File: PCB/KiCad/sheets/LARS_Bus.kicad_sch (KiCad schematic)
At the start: 24 parts, among them J27 USB1, J28 USB2, U11 USBLC6-2SC6, U12 TCAN1057AVDRQ1, U13 USBLC6-2SC6

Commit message: reannotate schematic
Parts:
- renumbered C63 to C65, C64 to C66, C65 to C67, J27 to J28, J28 to J29, U11 to U10, U12 to U11, U13 to U12
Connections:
- net CAN1_HIGH renamed CAN1_P
- net CAN1_LOW renamed CAN1_N

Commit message: finish PCB routing
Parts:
- C67: value 1u -> 2u2
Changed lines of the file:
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@@
 			)
 		)
-		(property "Value" "1u"
+		(property "Value" "2u2"
 			(at 98.298 148.082 0)
 			(effects

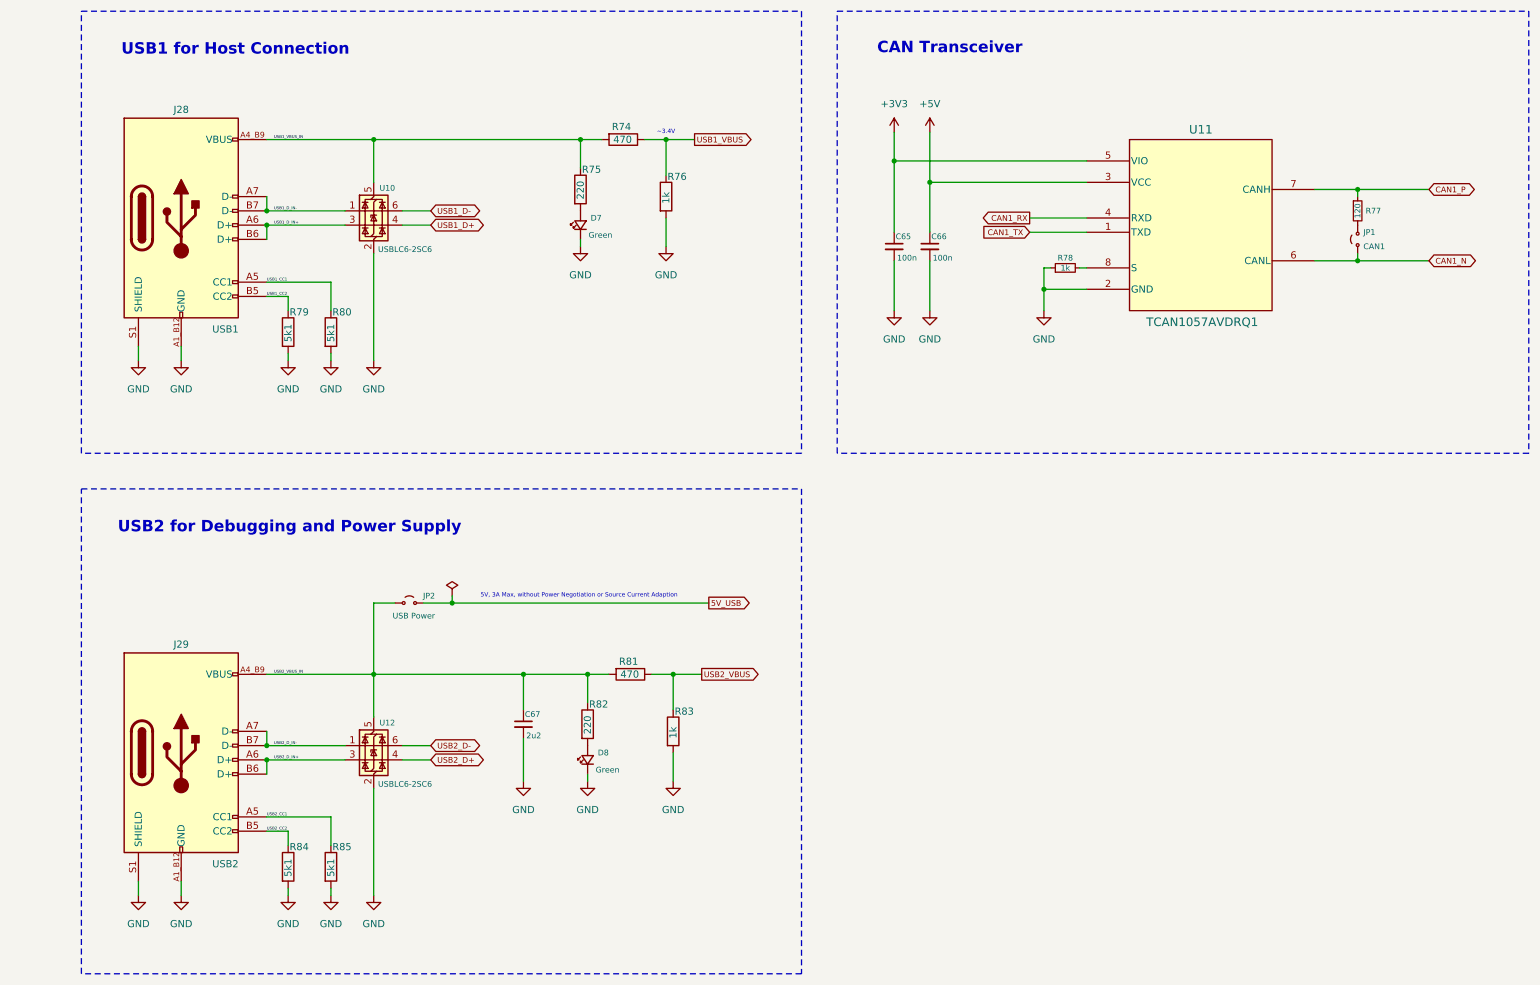
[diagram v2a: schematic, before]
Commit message: change default KiCad schematic font
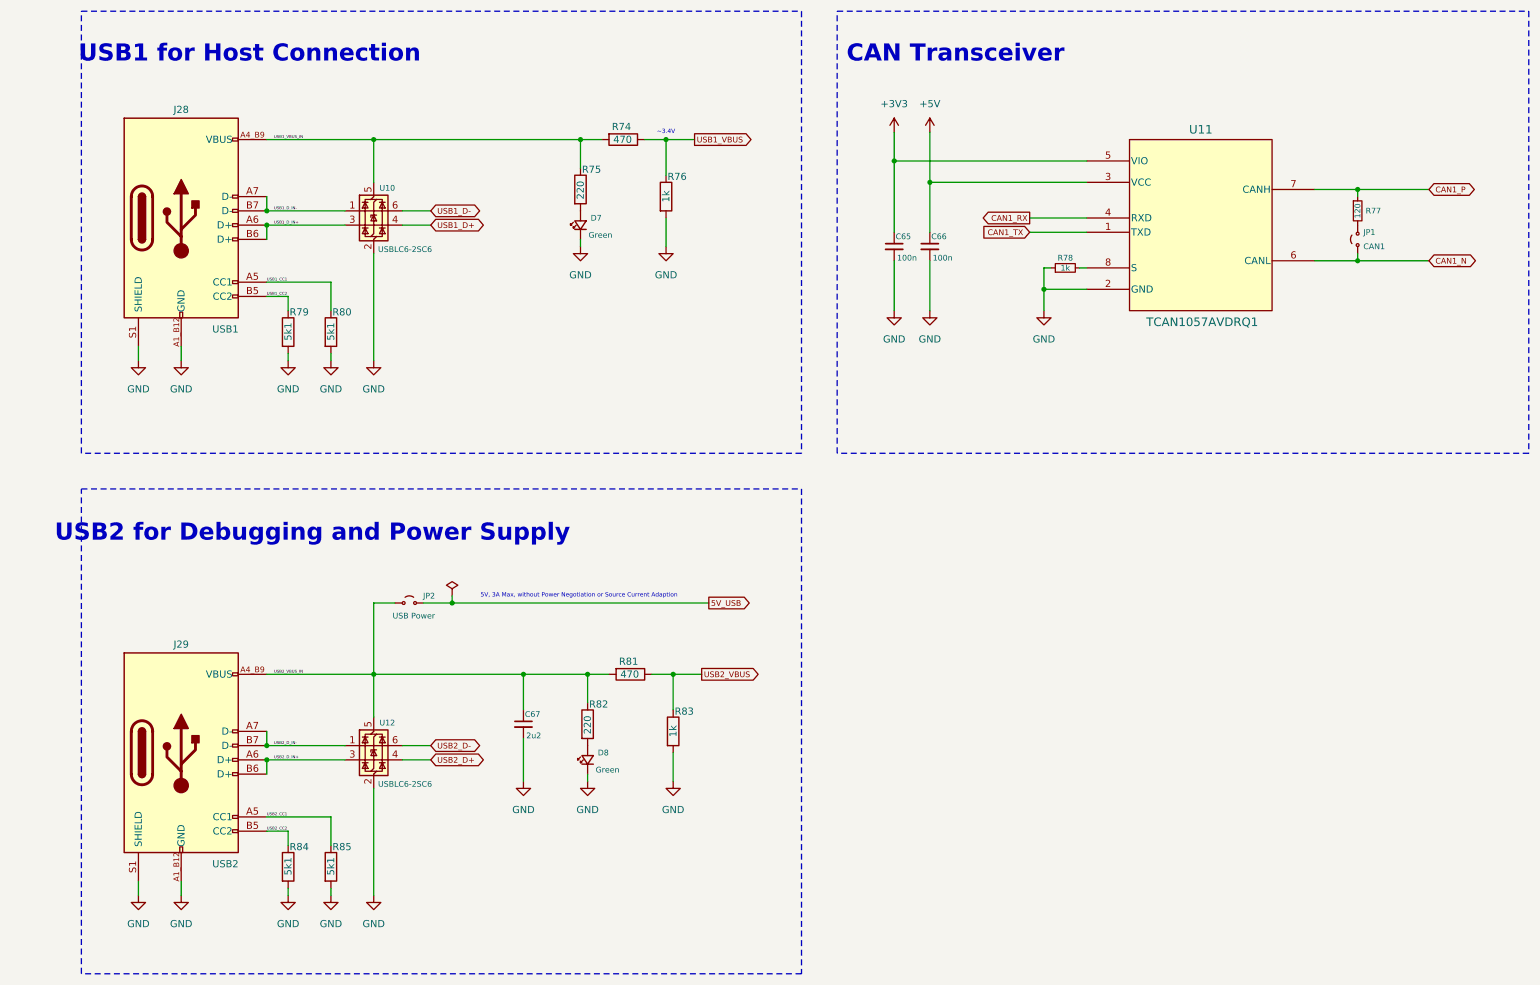
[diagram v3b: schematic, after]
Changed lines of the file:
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@@
 	(text "CAN Transceiver"
 		(exclude_from_sim no)
-		(at 173.736 25.654 0)
+		(at 174.752 26.67 0)
 		(effects
 			(font
-				(size 2.032 2.032)
+				(size 3.048 3.048)
 				(thickness 0.4064)
 				(bold yes)
@@
 	(text "USB2 for Debugging and Power Supply"
 		(exclude_from_sim no)
-		(at 56.134 110.998 0)
+		(at 60.198 112.014 0)
 		(effects
 			(font
-				(size 2.032 2.032)
+				(size 3.048 3.048)
 				(thickness 0.4064)
 				(bold yes)
@@
 	(text "USB1 for Host Connection"
 		(exclude_from_sim no)
-		(at 46.482 25.908 0)
+		(at 49.022 26.67 0)
 		(effects
 			(font
-				(size 2.032 2.032)
+				(size 3.048 3.048)
 				(thickness 0.4064)
 				(bold yes)
@@
 		)
 		(property "Value" "5k1"
-			(at 55.88 173.228 90)
+			(at 55.88 172.974 90)
 			(effects
 				(font
@@
 		)
 		(property "Value" "1k"
-			(at 124.46 148.59 90)
+			(at 124.46 148.336 90)
 			(effects
 				(font
@@
 		)
 		(property "Value" "5k1"
-			(at 63.5 77.978 90)
+			(at 63.5 77.724 90)
 			(effects
 				(font
@@
 		)
 		(property "Value" "1k"
-			(at 123.19 53.34 90)
+			(at 123.19 53.086 90)
 			(effects
 				(font
@@
 		)
 		(property "Value" "5k1"
-			(at 63.5 173.228 90)
+			(at 63.5 172.974 90)
 			(effects
 				(font
@@
 		)
 		(property "Value" "5k1"
-			(at 55.88 77.978 90)
+			(at 55.88 77.724 90)
 			(effects
 				(font

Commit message: update text layout and fix remaining DRC errors
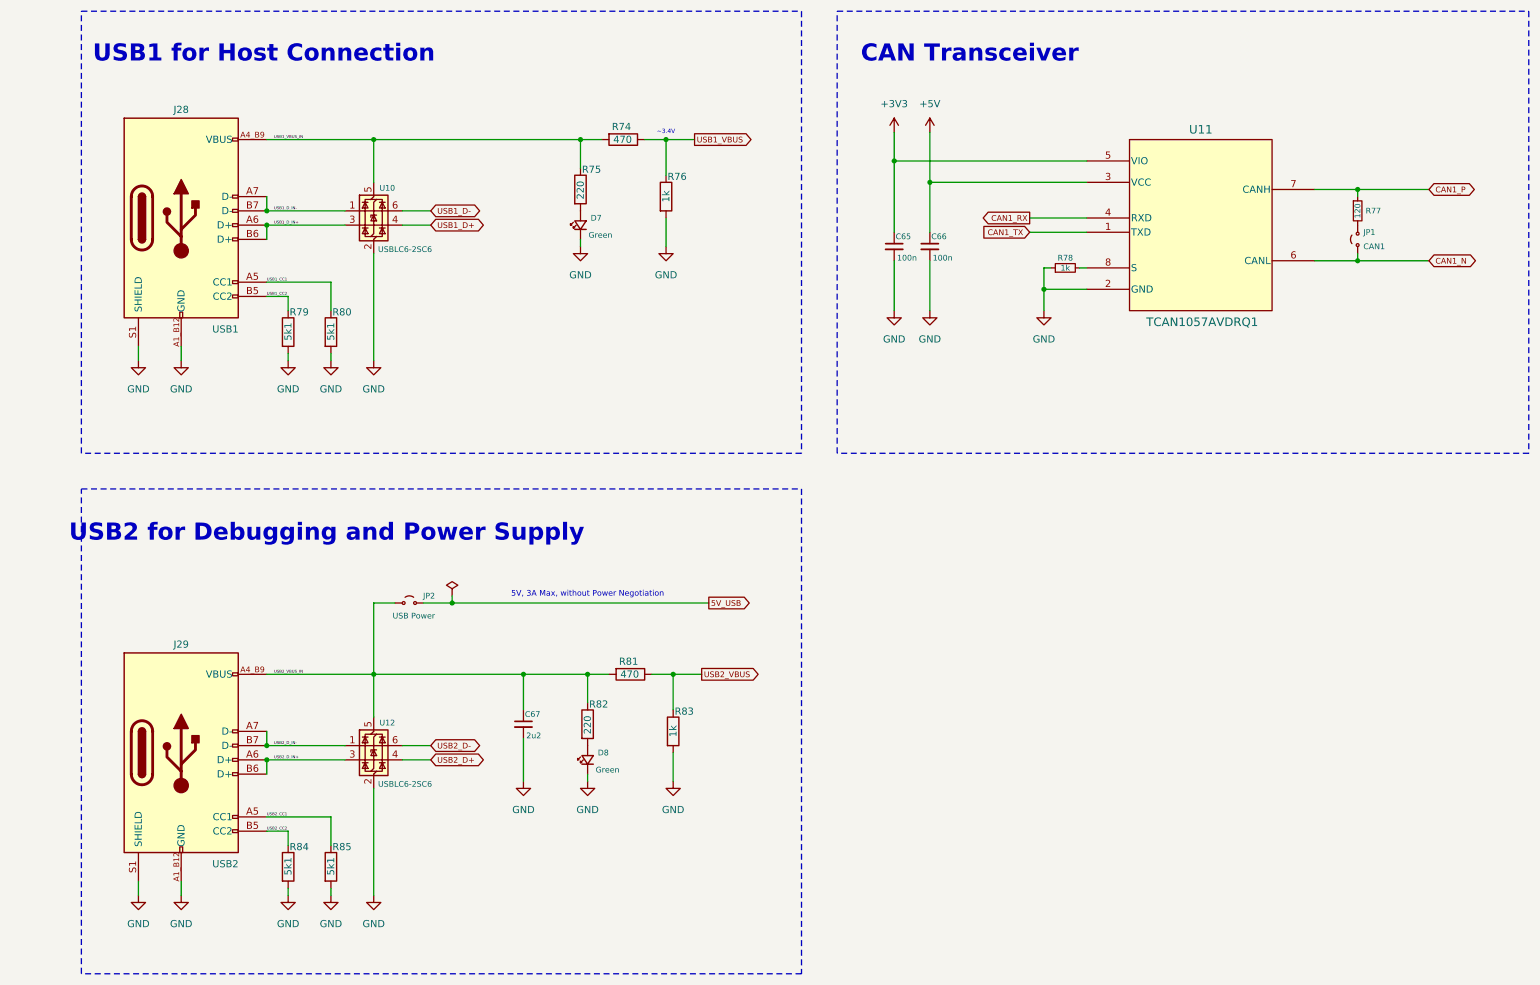
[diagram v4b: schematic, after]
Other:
- note added: "5V, 3A Max, without Power Negotiation"
- note removed: "5V, 3A Max, without Power Negotiation or Source Current Adaption"
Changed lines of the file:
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@@
 	(text "CAN Transceiver"
 		(exclude_from_sim no)
-		(at 174.752 26.67 0)
+		(at 177.292 26.67 0)
 		(effects
 			(font
@@
 		)
 	)
-	(text "5V, 3A Max, without Power Negotiation or Source Current Adaption"
+	(text "5V, 3A Max, without Power Negotiation"
 		(exclude_from_sim no)
-		(at 107.696 123.19 0)
+		(at 109.22 122.936 0)
 		(effects
 			(font
-				(size 0.762 0.762)
+				(size 1.016 1.016)
 			)
 		)
@@
 	(text "USB2 for Debugging and Power Supply"
 		(exclude_from_sim no)
-		(at 60.198 112.014 0)
+		(at 62.738 112.014 0)
 		(effects
 			(font
@@
 	(text "USB1 for Host Connection"
 		(exclude_from_sim no)
-		(at 49.022 26.67 0)
+		(at 51.562 26.67 0)
 		(effects
 			(font
